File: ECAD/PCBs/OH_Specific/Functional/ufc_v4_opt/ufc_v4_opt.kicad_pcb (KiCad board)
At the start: 2 copper layers, 43 x 12 mm, 71 parts, among them J1 Conn_01x05_Male, J2 Conn_01x05_Male, J3 Conn_01x05_Male, J4 Conn_01x05_Male

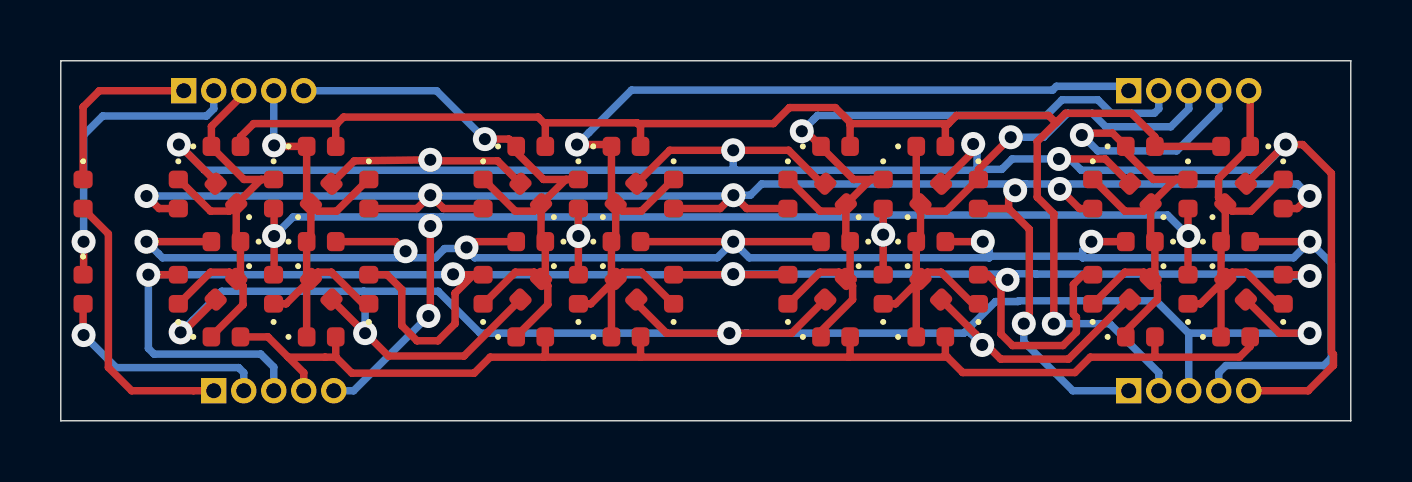
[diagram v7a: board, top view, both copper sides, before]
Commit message: Updated PCBs to use 0.45mm/0.2mm vias updated gerber files for all modified boards. added panelzed gerber files
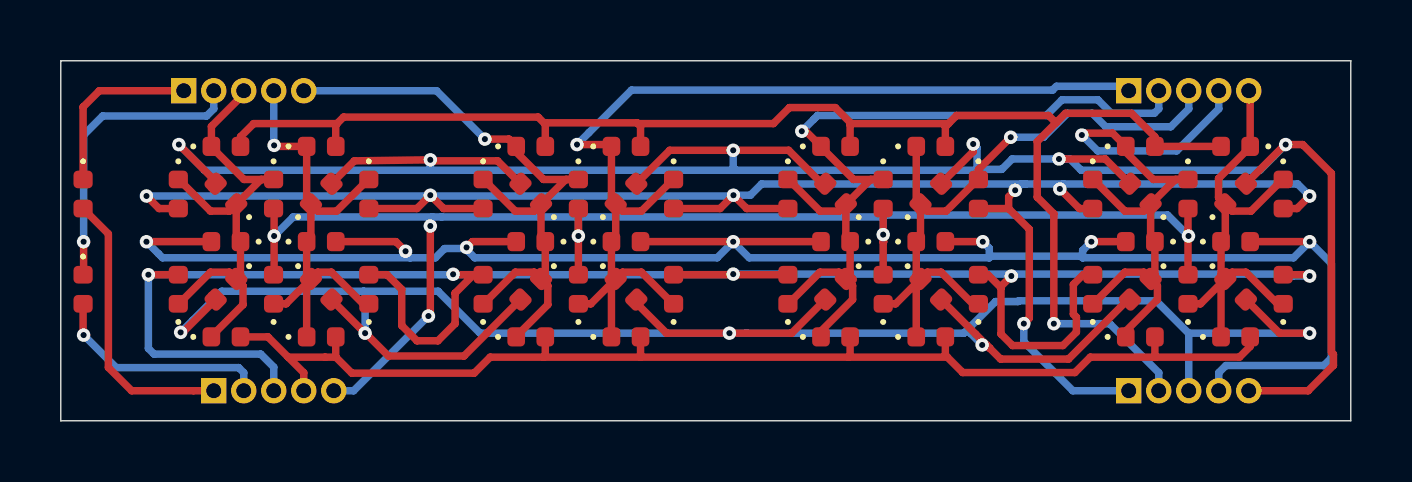
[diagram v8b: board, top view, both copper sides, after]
